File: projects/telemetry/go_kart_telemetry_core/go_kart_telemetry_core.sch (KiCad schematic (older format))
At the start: 57 parts, among them J1 MM_F_RA_20, J2 JST_SM06B-GHS-TB_LF__SN_, J3 CONN_02X03, U1 ATMEGA16M1, U2 TPS560430YF, U3 MCP79511-I_MS, U4 TXB0104PW, U5 LM3480-3.3, U6 MCP2561-E_SN, Y1 Crystal_SMD, Y2 Crystal_32_768kHz

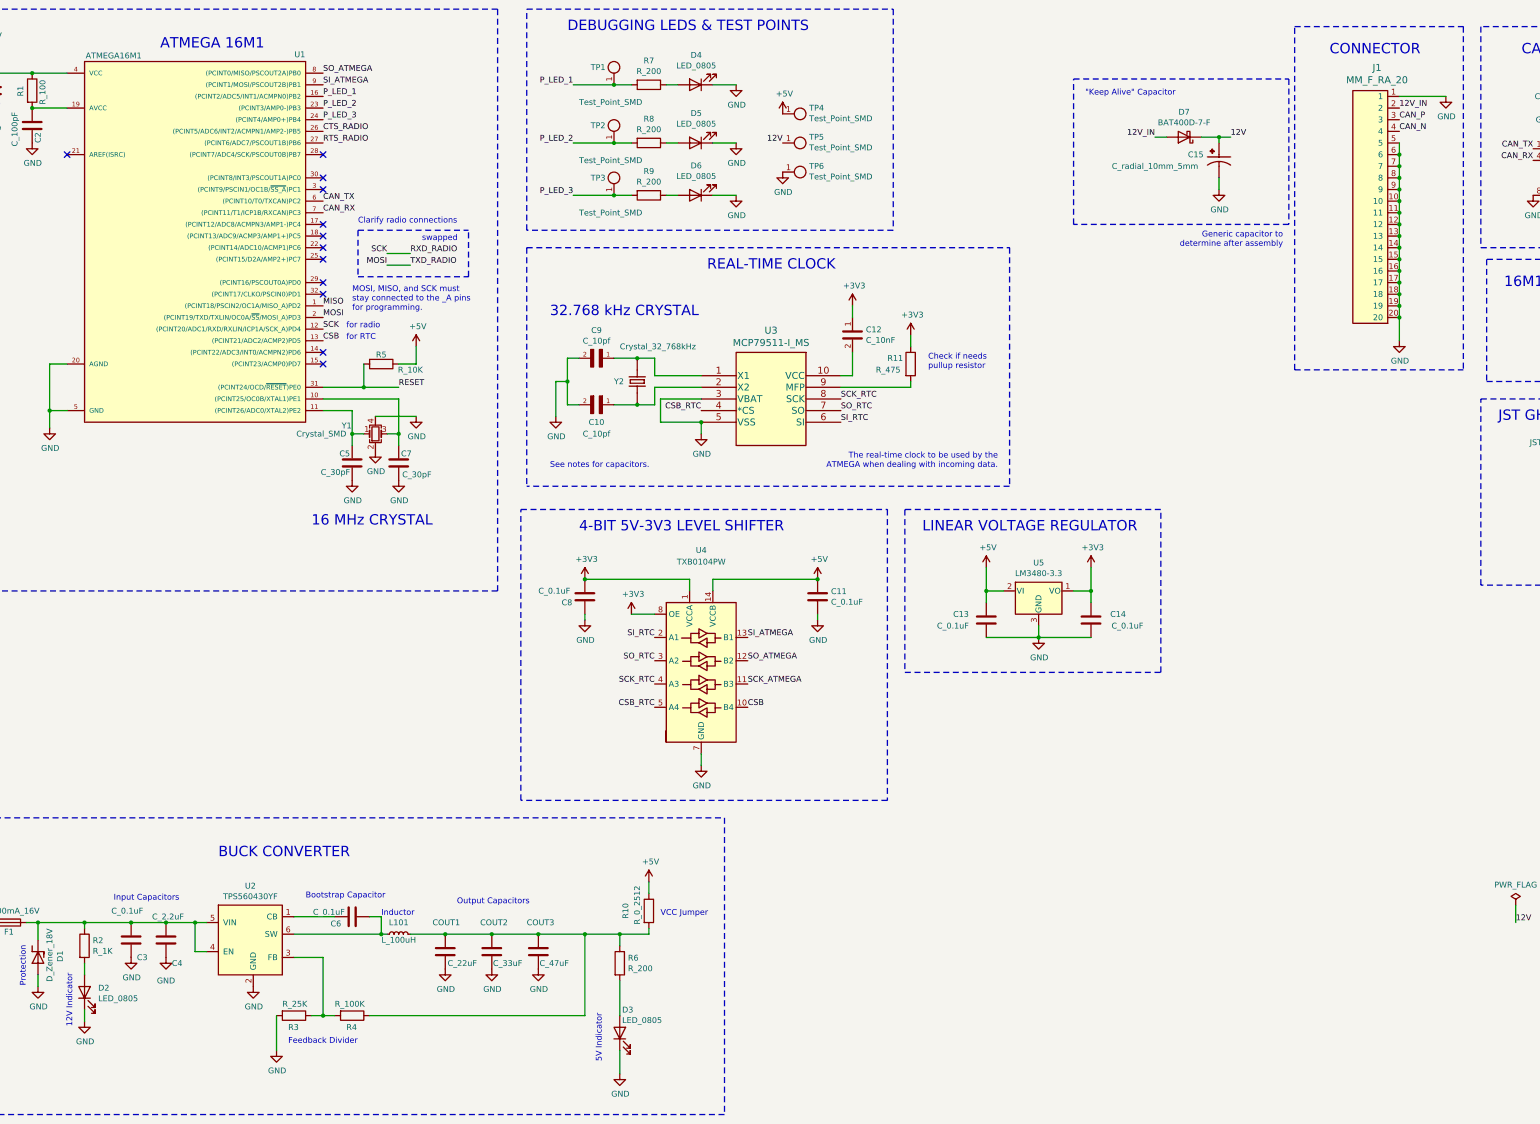
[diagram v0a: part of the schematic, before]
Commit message: feat: begin changes from mk5 schematic
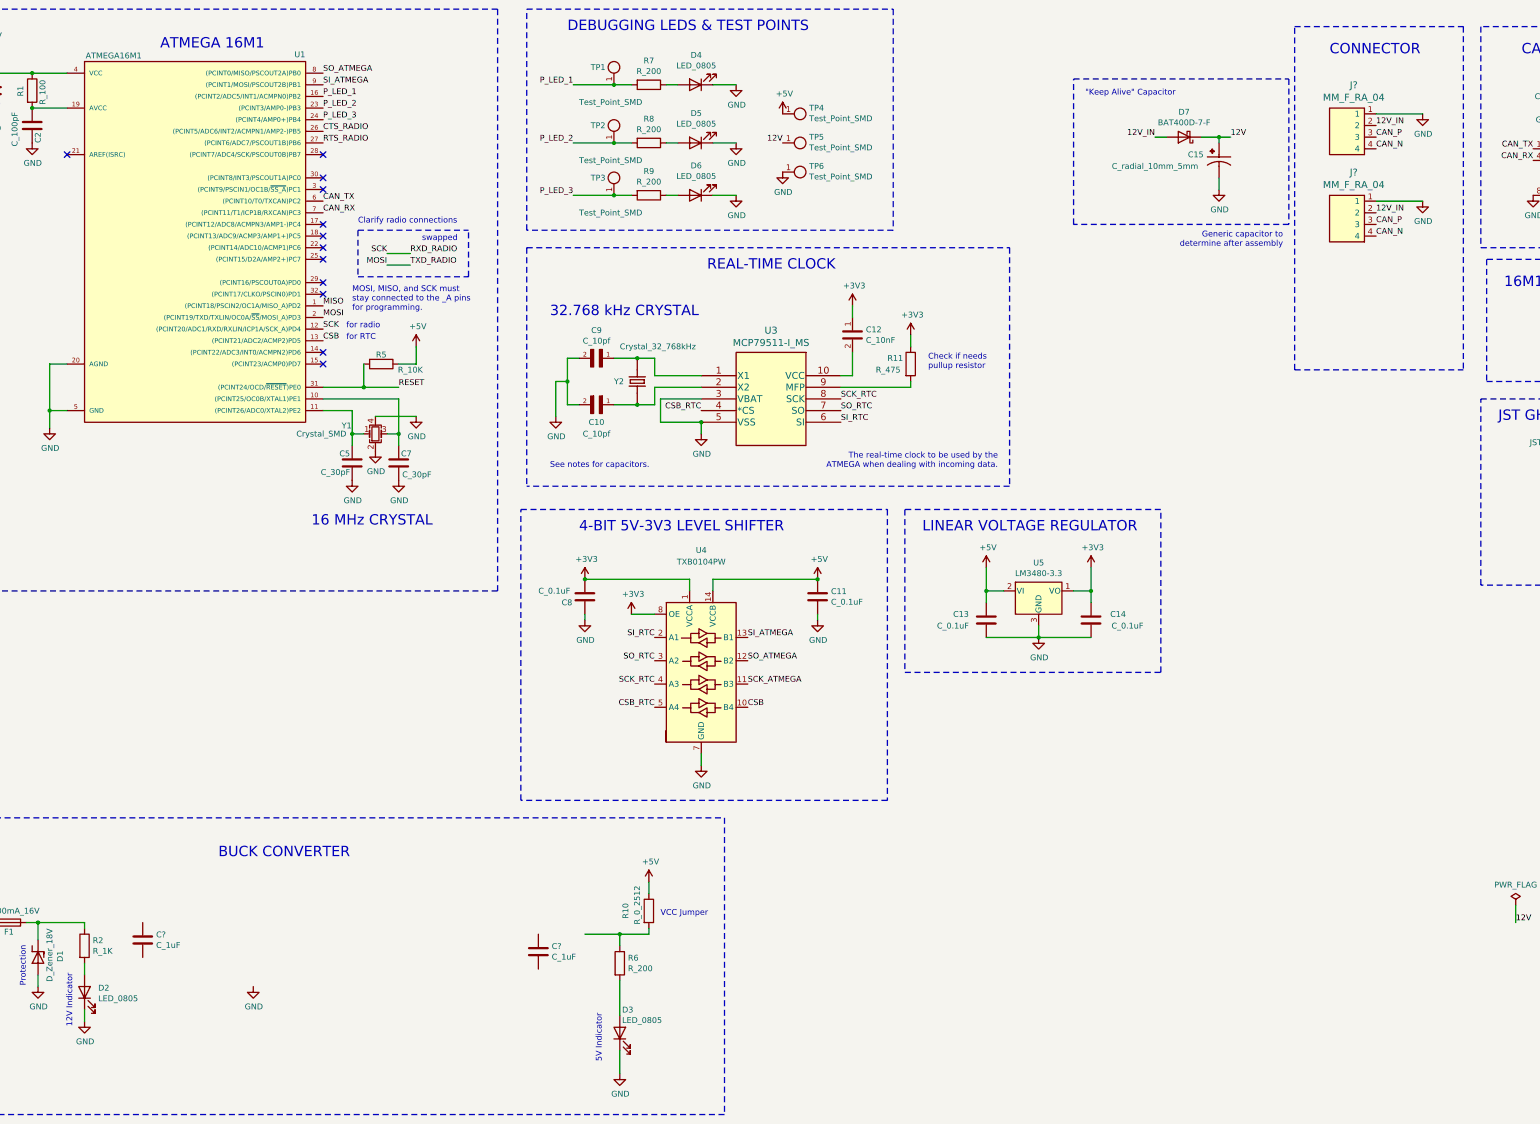
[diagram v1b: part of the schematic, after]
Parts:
- removed C3, C6: C_0.1uF, footprints:C_0805_OEM, symbol formula:C_0.1uF
- removed C4: C_2.2uF, footprints:C_0603_1608Metric, symbol formula:C_2.2uF
- removed COUT1: C_22uF, footprints:C_1206_OEM, symbol formula:C_22uF
- removed COUT2: C_33uF, footprints:Fuse_1812, symbol formula:C_33uF
- removed COUT3: C_47uF, footprints:C_0805_OEM, symbol formula:C_47uF
- removed J1: MM_F_RA_20, footprints:micromatch_female_ra_20, symbol formula:MM_F_RA_20
- removed L101: L_100uH, footprints:L_100uH_OEM, symbol formula:L_100uH
- removed R3: R_25K, footprints:R_0805_OEM, symbol formula:R_25K
- removed R4: R_100K, footprints:R_0805_OEM, symbol formula:R_100K
- removed U2: TPS560430YF, footprints:SOT-23-6_OEM, symbol formula:TPS560430YF
- added C? (x2): C_1uF, footprints:C_0805_OEM, symbol formula:C_1uF
- added J? (x2): MM_F_RA_04, footprints:micromatch_female_ra_4, symbol formula:MM_F_RA_04
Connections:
- net 12V_IN: now also J?.2, J?.2
- net CAN_N: now also J?.4, J?.4
- net CAN_P: now also J?.3, J?.3
- net GND: now also J?.1, J?.1
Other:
- note removed: "Bootstrap Capacitor\n"
- note removed: "Feedback Divider\n"
- note removed: "Inductor\n"
- note removed: "Input Capacitors\n\n"
- note removed: "Output Capacitors\n"

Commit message: feat: begin changes for gokart
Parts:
- added U2: AP7370, footprints:SOT-23-5, symbol formula:AP7370
- gave numbers to parts that had none: 4
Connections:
- net GND: now also C3.2, C4.2, U2.2 (GND)
- net at D1.1 (K), F1.1, R2.1: now also C3.1, U2.1 (Vin)
- net at R10.2, R6.1: now also C4.1, U2.5 (Vout)
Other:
- note added: "5V Linear Voltage Regulator\n"
- note added: "CONNECTORS"
- note added: "Input Capacitor"
- note added: "Output Capacitor"
- note removed: "BUCK CONVERTER\n"
- note removed: "CONNECTOR"
- moved on the sheet: C3, C4, D1, D2, D3, F1, R10, R2, R6
